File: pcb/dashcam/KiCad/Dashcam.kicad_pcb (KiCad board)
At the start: 2 copper layers, 60 x 58.8 mm, 28 parts, among them J3 Conn_02x03_Odd_Even, J4 Conn_01x08_Pin, SW1 SW_Push, U1 WS2812B, U2 BC547, U3 ATTINY85-20SU, U4 WS2812B

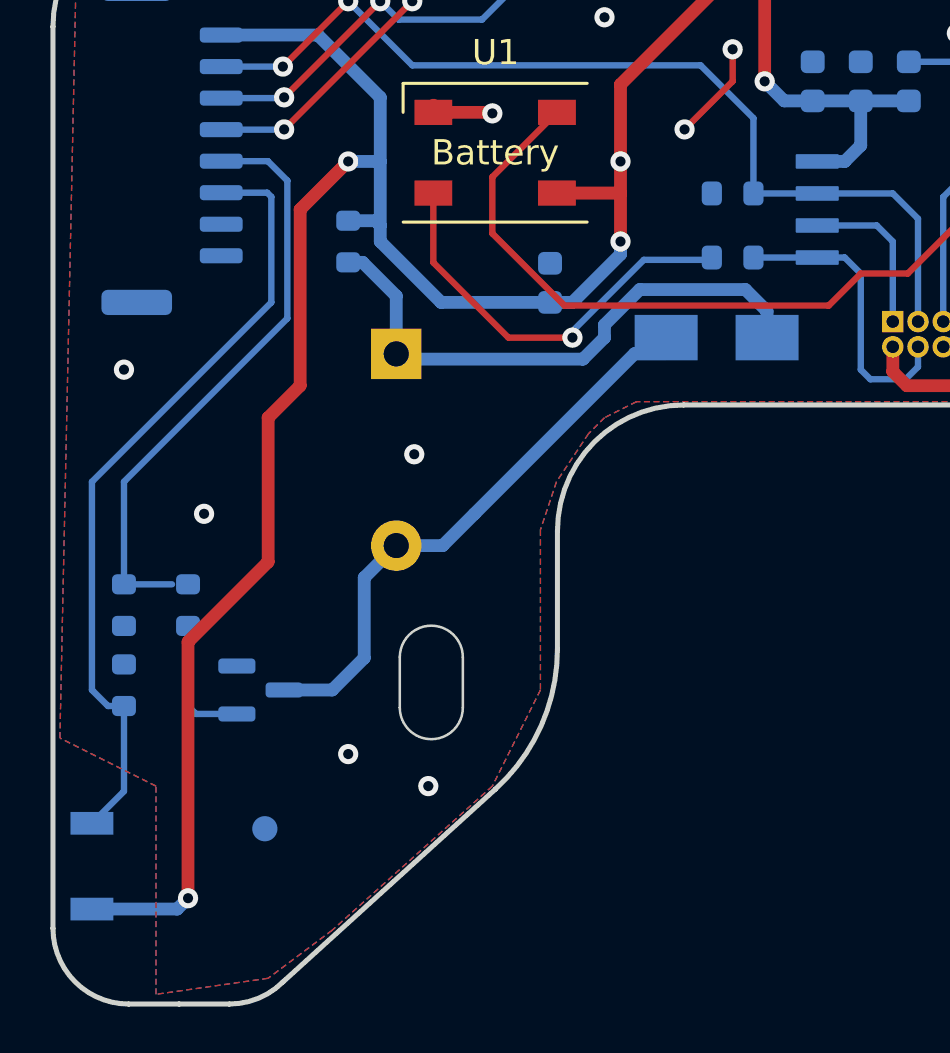
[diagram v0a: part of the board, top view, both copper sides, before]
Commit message: diode removed added cap to push reset ckt
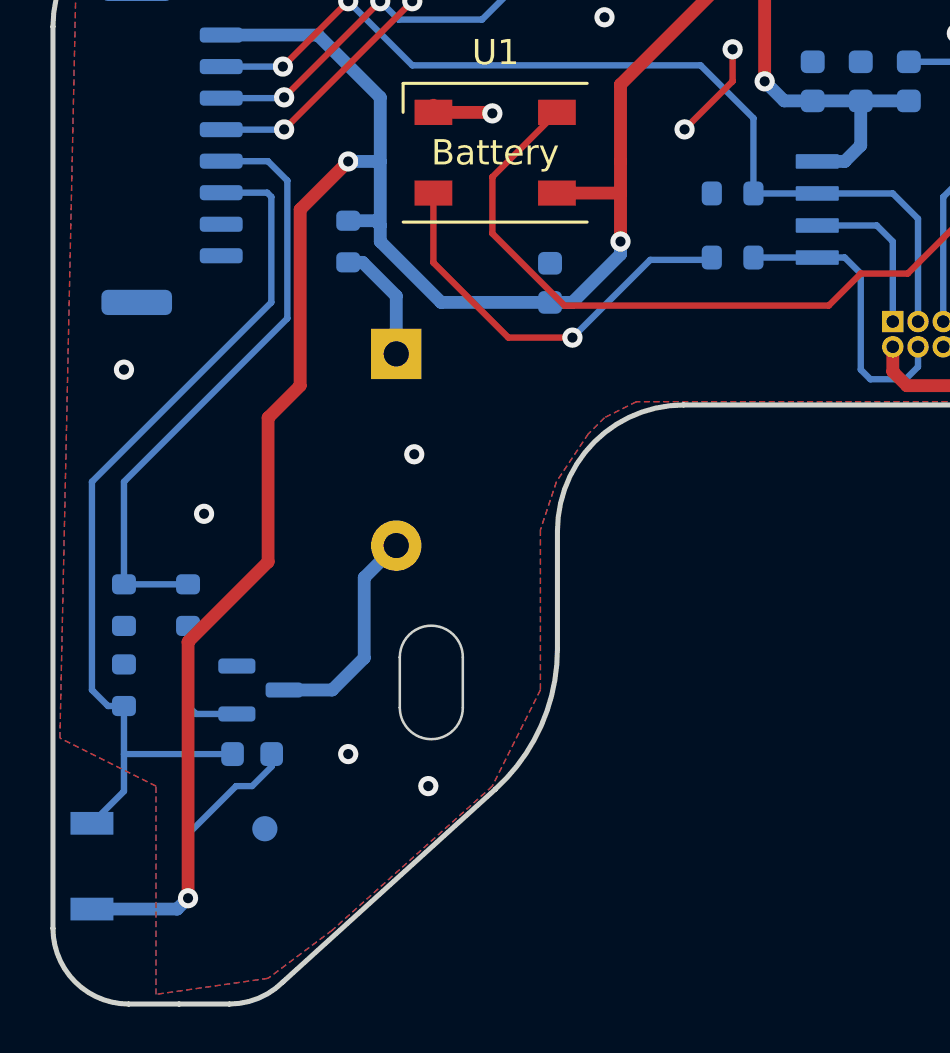
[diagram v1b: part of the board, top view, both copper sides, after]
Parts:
- removed D3: 1N4007, Diode_SMD:D_SMA
- added C1: 100nF, Capacitor_SMD:C_0603_1608Metric, B.Cu at (115.8, 80.3)
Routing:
- net Net-(BZ1--): track 23.0 -> 5.17 mm
- net Net-(BZ1-+): track 23.2 -> 9.32 mm
- net +5V: track 167.3 -> 174.7 mm, vias 7 -> 6
- net pushbutton: track 31.3 -> 35.6 mm
- net buzzer: track 23.5 -> 24.2 mm

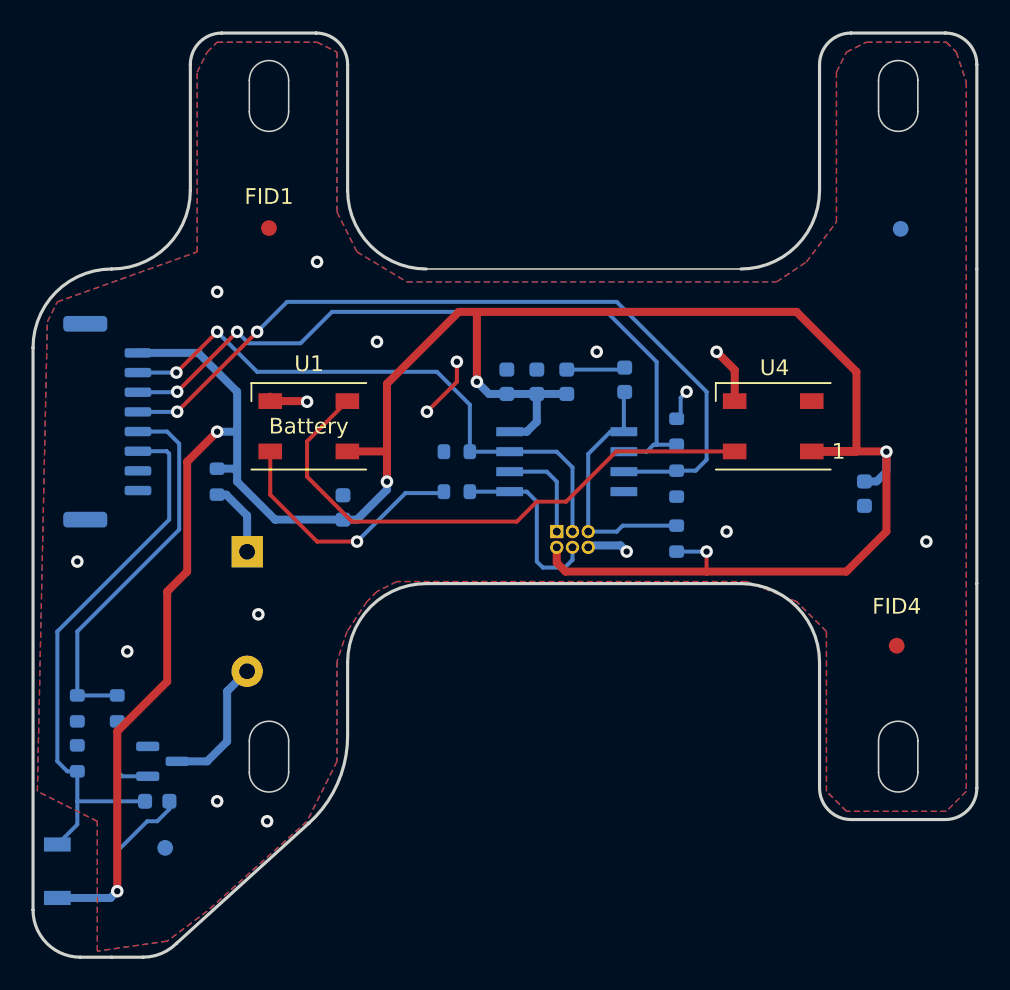
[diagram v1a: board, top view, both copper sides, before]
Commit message: pcb- pulldown removed, 470 ohm added in series
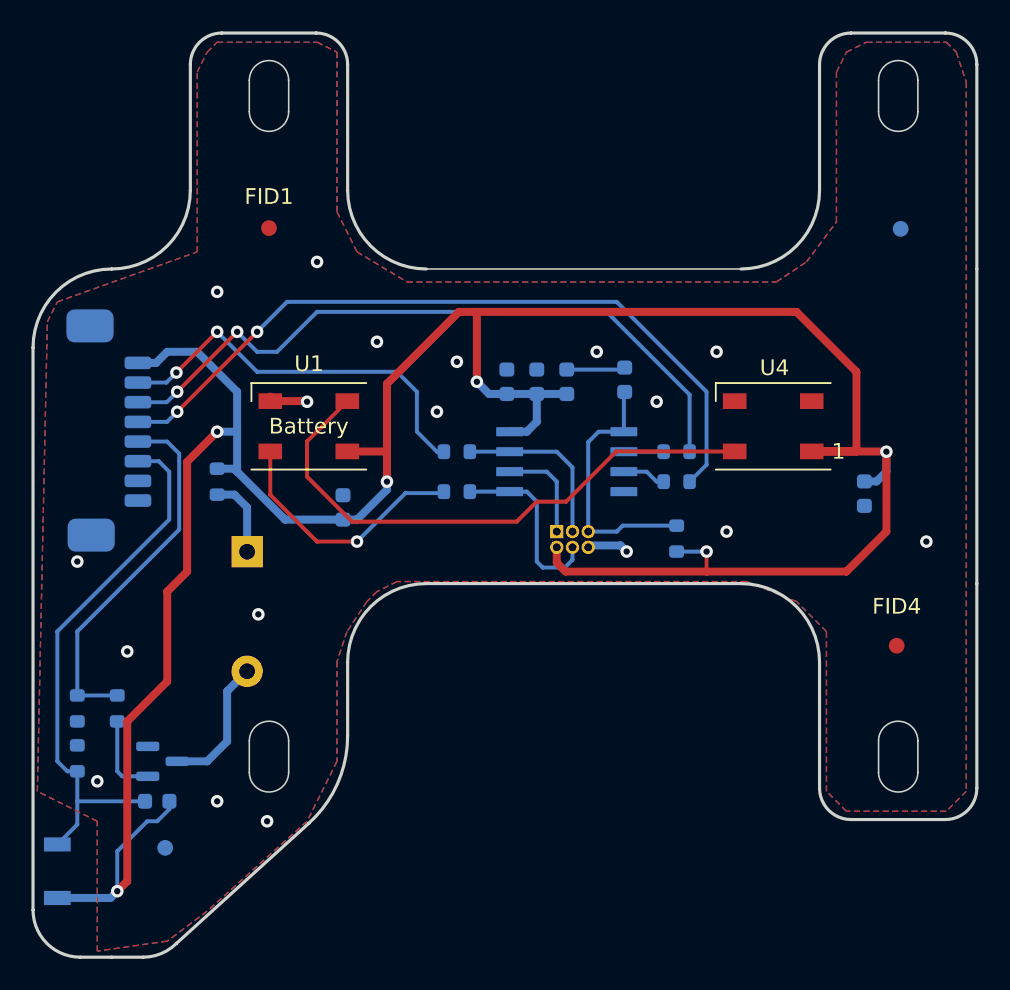
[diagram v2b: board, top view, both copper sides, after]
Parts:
- R7, R8, R9: value 10k -> 470R
- moved R9 3.18 mm to (148.8, 60.0), turned to 0 degrees
- moved R8 2.03 mm to (148.8, 58.1), turned to 0 degrees
- moved J4 0.63 mm to (112.6, 56.8)
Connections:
- J3 pad 3: LED Selector -> SEK
- R7 pad 1: GND -> LED Selector
- R7 pad 2: LED Selector -> SEK
- R8 pad 1: GND -> Net-(U3-PB3)
- R8 pad 2: ValuePin_2 -> ValuePin_1
- R9 pad 1: GND -> Net-(U3-PB4)
- R9 pad 2: ValuePin_1 -> ValuePin_2
- U3 pad 2: ValuePin_1 -> Net-(U3-PB3)
- U3 pad 3: ValuePin_2 -> Net-(U3-PB4)
- U3 pad 7: LED Selector -> SEK
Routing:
- net LED Selector: track 38.2 -> 25.5 mm
- net SEK: track 0.00 -> 11.0 mm
- net GND: track 18.9 -> 9.43 mm, vias 17 -> 18
- net ValuePin_2: track 51.3 -> 47.9 mm
- net Net-(U3-PB4): track 0.00 -> 2.79 mm
- net Net-(U3-PB3): track 0.00 -> 2.53 mm
- net ValuePin_1: track 46.1 -> 44.3 mm
- net pushbutton: track 35.6 -> 34.6 mm
- net buzzer: track 24.2 -> 23.5 mm

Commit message: added gerber files and changed 2x3 connector
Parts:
- J3: footprint Connector_PinHeader_1.00mm:PinHeader_2x03_P1.00mm_Vertical -> Connector_PinHeader_2.54mm:PinHeader_2x03_P2.54mm_Vertical
- moved J3 16.7 mm to (157.9, 64.0), turned to 90 degrees
- moved R3 12.0 mm to (160.8, 64.1)
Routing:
- net MISO: track 6.43 -> 25.9 mm, vias 0 -> 1
- net +5V: track 174.6 -> 155.6 mm, vias 6 -> 5
- net SEK: track 11.0 -> 25.4 mm
- net MOSI: track 11.8 -> 25.0 mm, vias 0 -> 1
- net Reset: track 16.6 -> 28.7 mm
- net GND: track 9.43 -> 6.51 mm, vias 18 -> 16
- net neodin: track 16.3 -> 18.0 mm
